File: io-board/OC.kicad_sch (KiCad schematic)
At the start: 4 parts, among them Q16 NPN

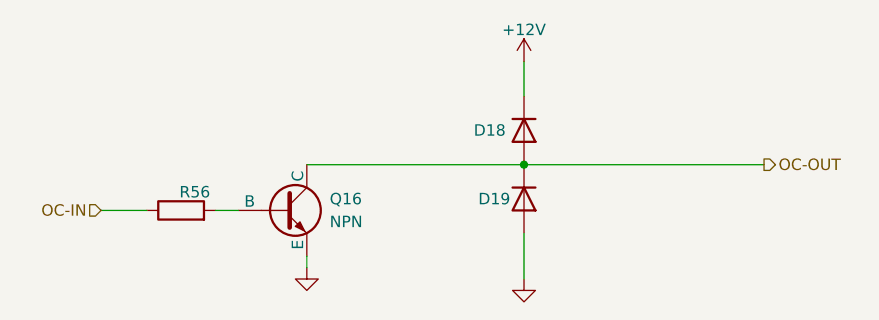
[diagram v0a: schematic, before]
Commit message: PCB: io-board: component values and BOM
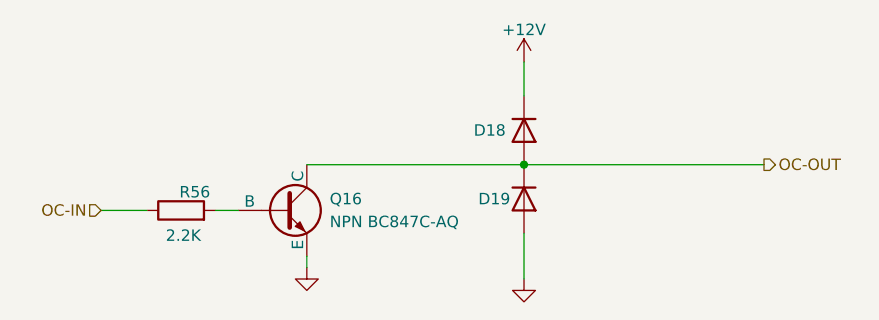
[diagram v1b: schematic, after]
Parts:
- D18, D19: value D -> Vishay MCL4448-TR
- Q16: value NPN -> NPN BC847C-AQ
- R56: value R -> 2.2K
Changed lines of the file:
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@@
 			)
 		)
-		(property "Value" "R"
-			(at 113.792 95.758 90)
-			(effects
-				(font
-					(size 1.27 1.27)
-				)
-				(hide yes)
+		(property "Value" "2.2K"
+			(at 115.824 100.584 90)
+			(effects
+				(font
+					(size 1.27 1.27)
+				)
 			)
 		)
@@
 			)
 		)
-		(property "Value" "D"
+		(property "Value" "Vishay MCL4448-TR"
 			(at 156.21 90.1699 90)
 			(effects
@@
 			)
 		)
-		(property "Value" "NPN"
+		(property "Value" "NPN BC847C-AQ"
 			(at 132.08 99.0599 0)
 			(effects
@@
 			)
 		)
-		(property "Value" "D"
+		(property "Value" "Vishay MCL4448-TR"
 			(at 156.21 97.7899 90)
 			(effects
